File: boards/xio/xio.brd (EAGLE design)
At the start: 170 x 170 mm, 390 parts, among them U2 LAN8742A-CZ, Y1 NX3225SA-12.000MHZ-STD-CSR-1, Y2 NX3225SA-12.000MHZ-STD-CSR-1, Y3 NX3225SA-25.000MHZ-STD-CSR-1

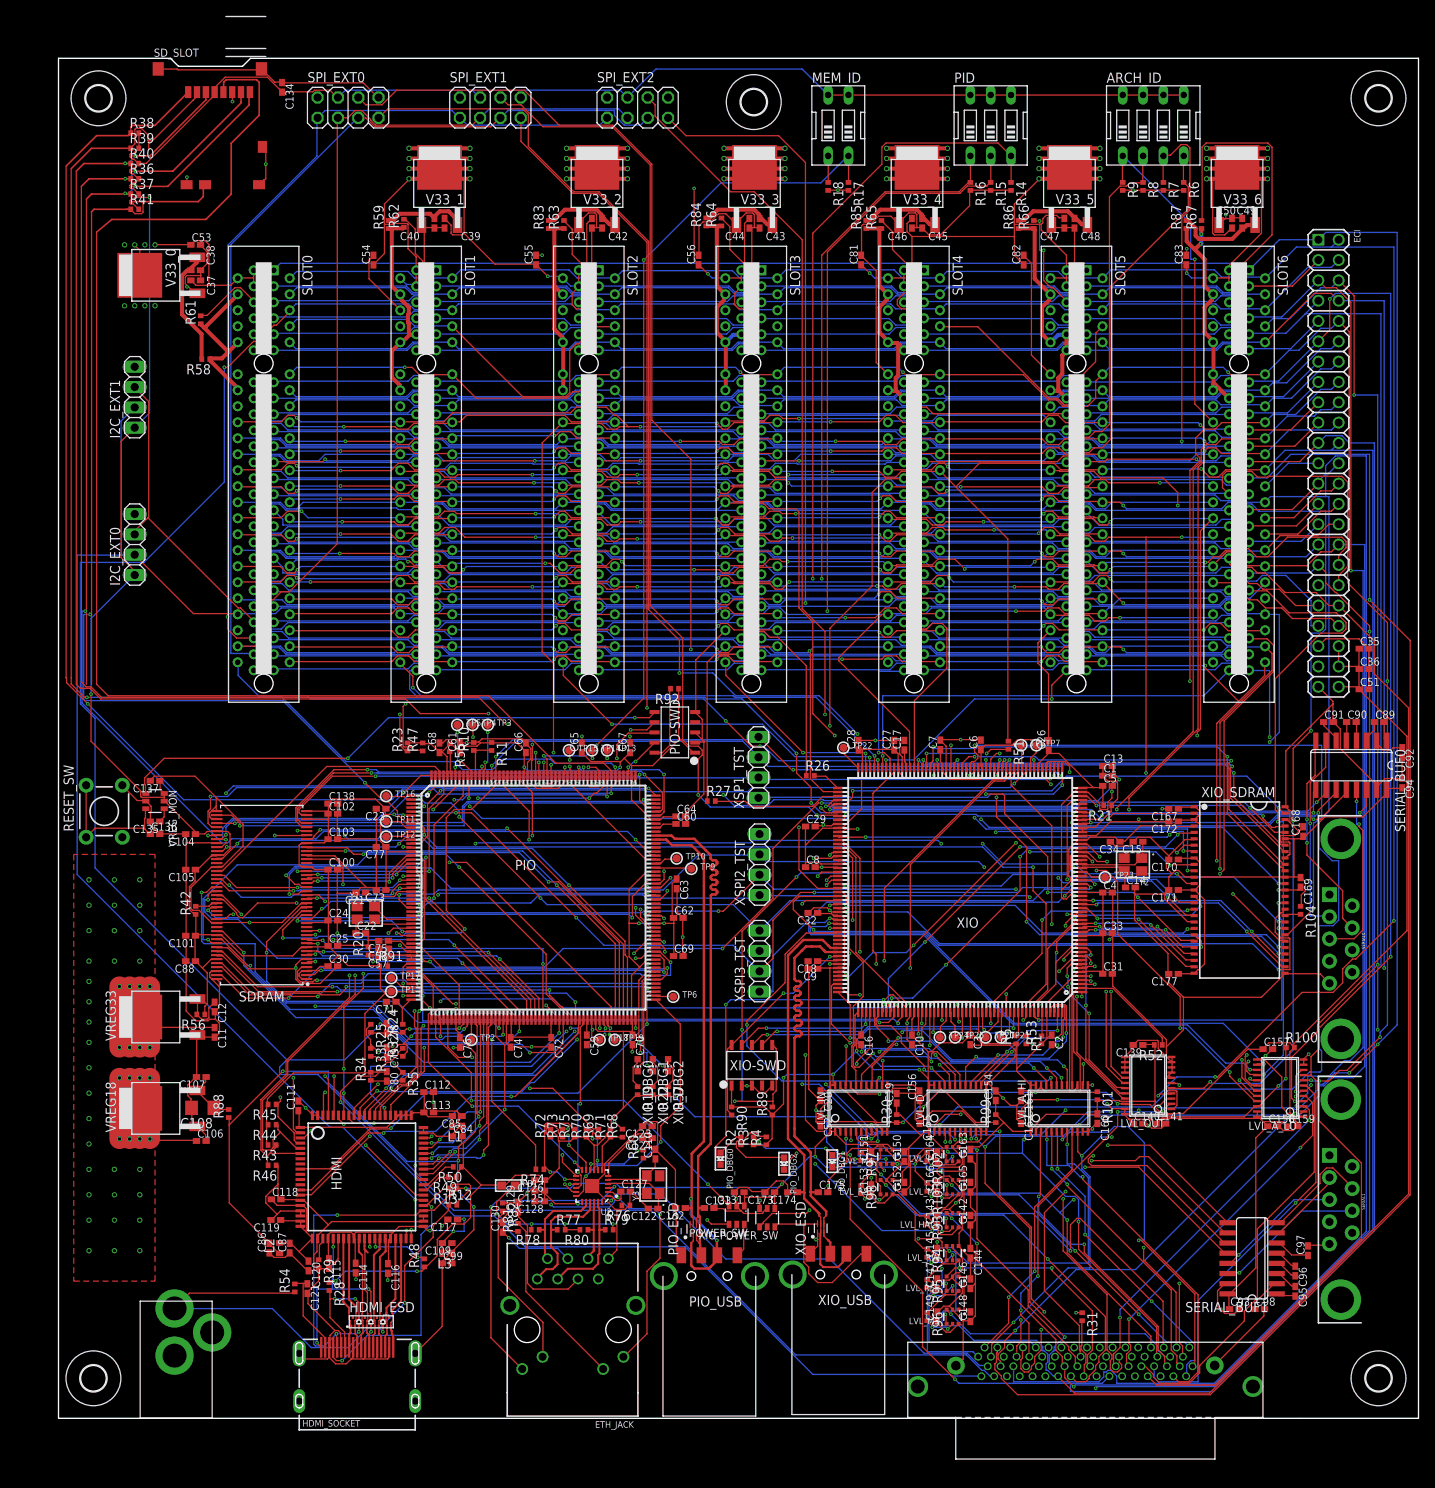
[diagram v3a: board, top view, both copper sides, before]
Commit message: Routed 6-layer board
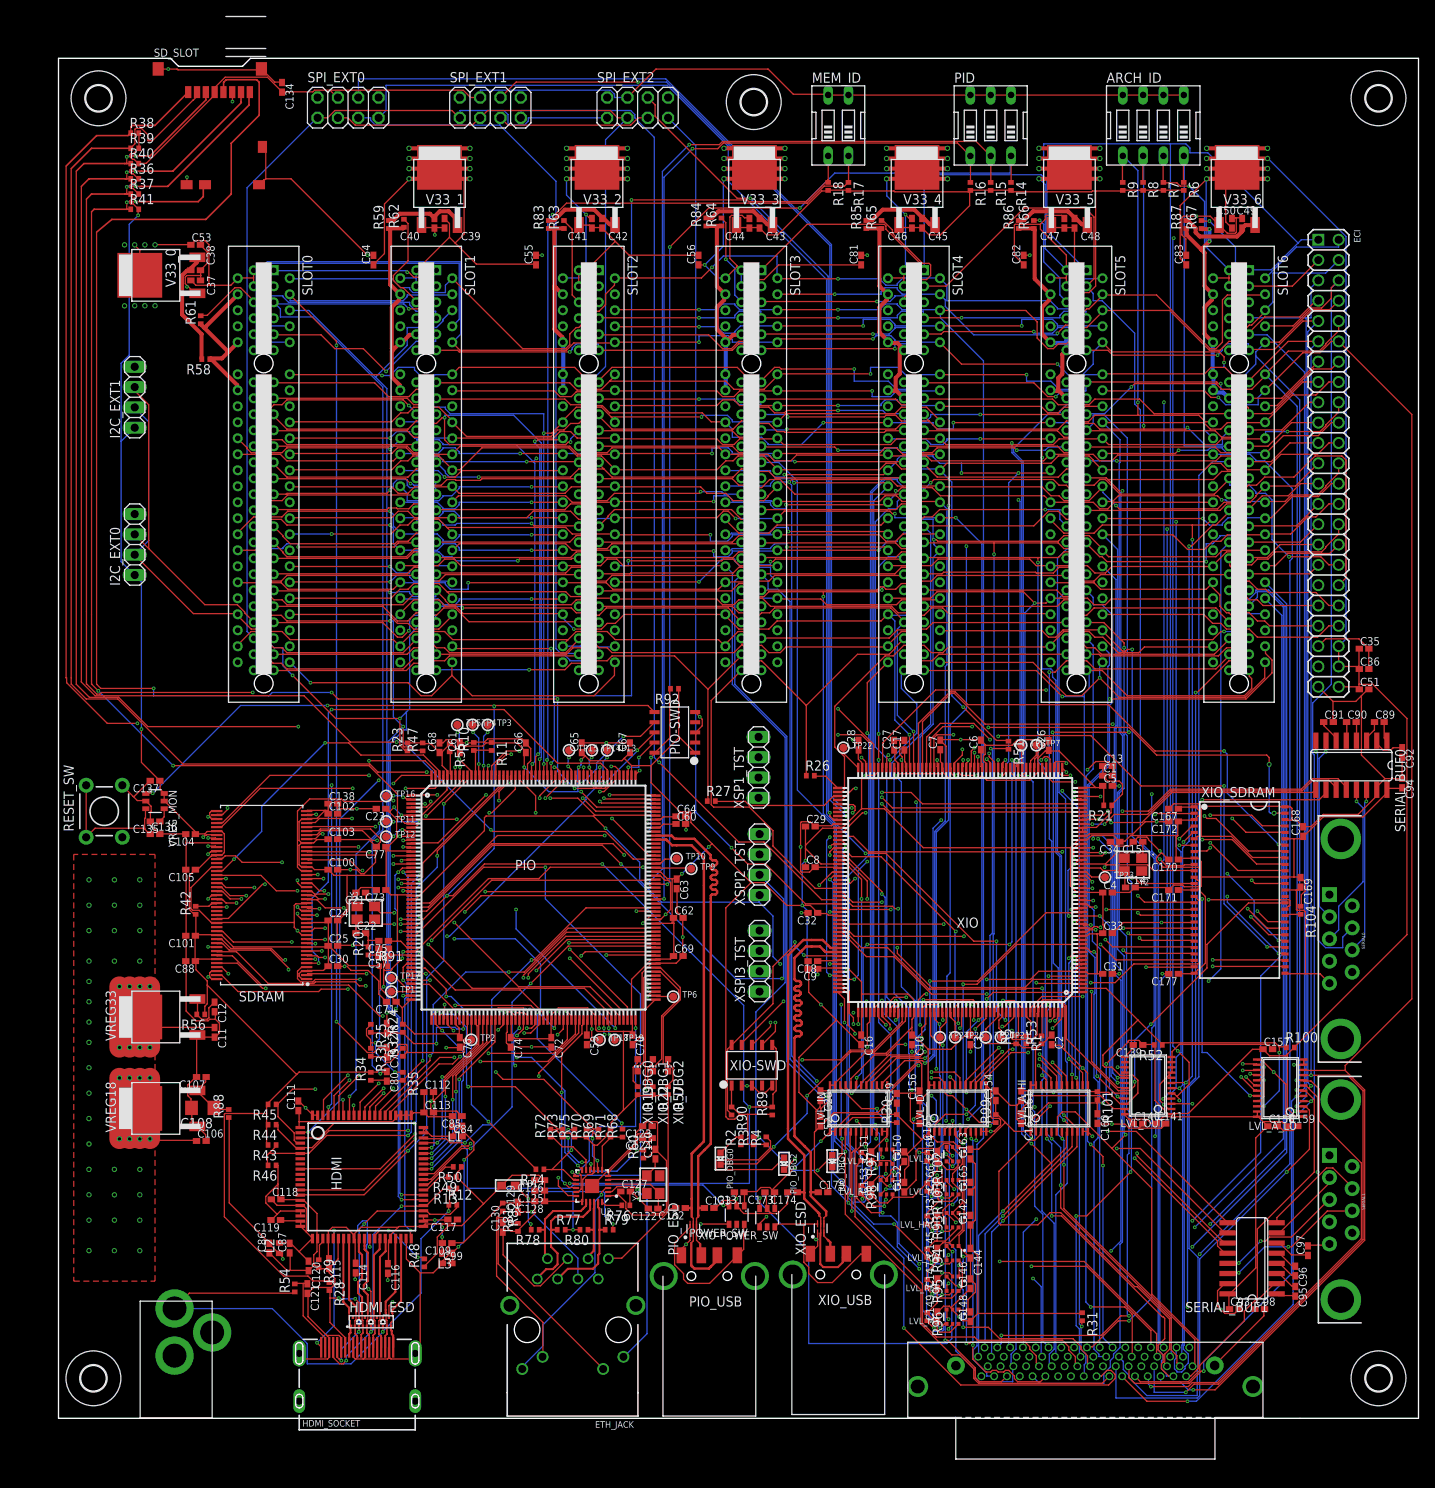
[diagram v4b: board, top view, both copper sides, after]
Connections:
- net GND: now also HDMI_ESD.P12; no longer HDMI_ESD.P18
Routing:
- net VHDCI_CCTL: track 346.4 -> 288.3 mm, vias 8 -> 3
- net VHDCI_CLK: track 328.5 -> 271.6 mm, vias 6 -> 4
- net VHDCI_COMMAND: track 305.3 -> 252.8 mm, vias 1 -> 4
- net VHDCI_D1: track 337.3 -> 288.2 mm, vias 1 -> 2
- net VHDCI_D0: track 301.8 -> 257.2 mm, vias 7 -> 5
- net I2C_SCL: track 314.0 -> 270.0 mm, vias 3 -> 6
- net VHDCI_HALT: track 294.2 -> 260.3 mm, vias 4 -> 2
- net GND: track 1203.2 -> 1169.5 mm, vias 75 -> 84
- net ETH_MDC: track 41.6 -> 73.2 mm
- net PSLOT6: track 40.0 -> 12.8 mm, vias 0 -> 1
- net VHDCI_A7: track 272.8 -> 299.9 mm, vias 1 -> 3
- net VHDCI_A3: track 292.9 -> 319.5 mm, vias 2 -> 5
- net VHDCI_A13: track 289.4 -> 263.4 mm, vias 7 -> 5
- net VHDCI_D4: track 268.8 -> 294.6 mm, vias 6 -> 3
- net VHDCI33_A9: track 62.1 -> 36.8 mm
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
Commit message: Big change.
Due to not being able to get the parts for the full system, we’re now just laying out the slots. We can add in the video and ethernet as cards rather than them being provided as-is.

This simplifies things a lot, now we only have 1 STM chip, and its associated SDRAM. The board is a lot smaller as well, and fits into 10cm in the Y dimension, which means making cards can be done using the cheap 10cm x 10cm board sizes that places like Seeed offer.

Need to define a cartridge port symbol, and remap all the pins to the STM32F746BGT6 (208 pin LQFP) which is available in China.

Assumption here is that the host-side will have an XPLA3 CPLD sitting on it, which manages the signal directionality under control of the STM, and also acts as a signal-buffer/level-translator. All signals on the expansion box are 3.3v apart from the 5v supply.

In the reverse direction, the STM ought to have sufficient juice to send the signals back on its own, since there’s only 1 load, and the signal path is short.
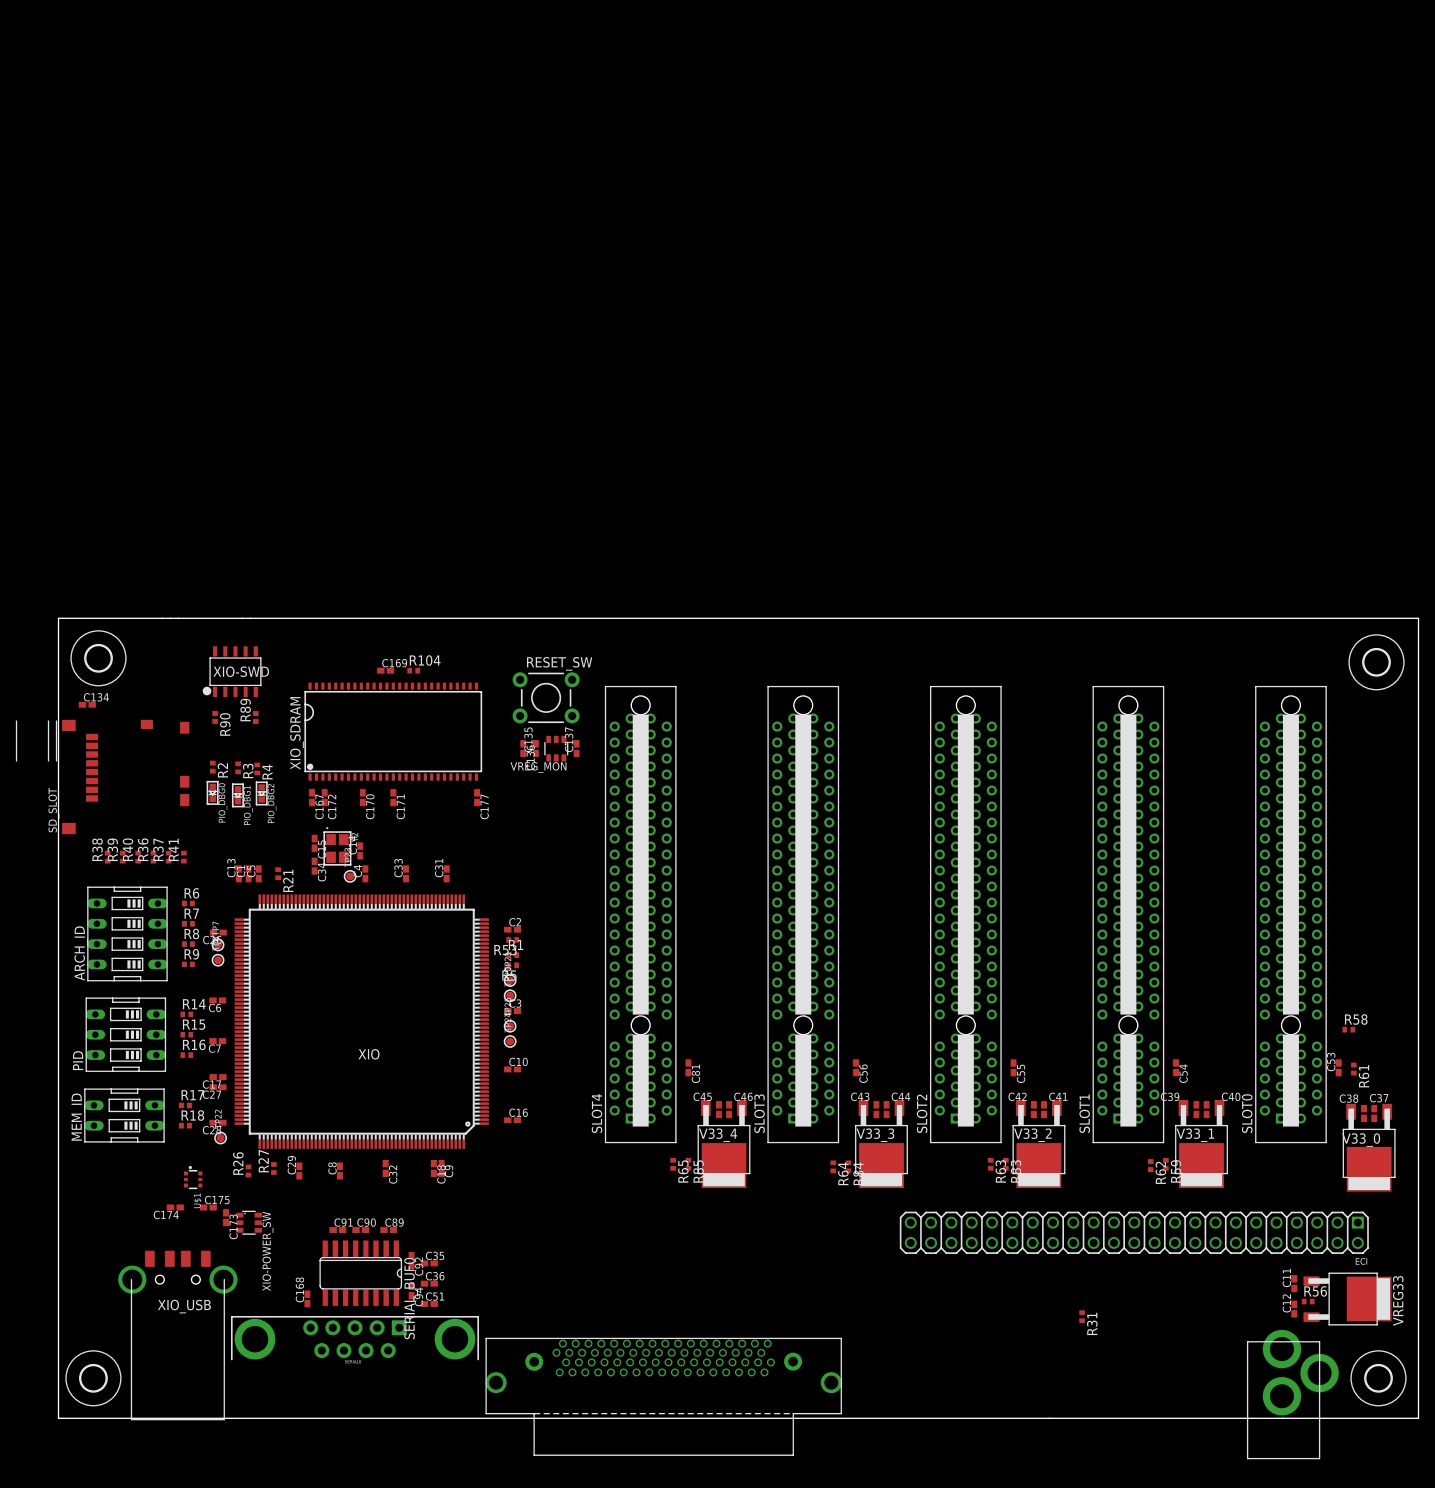
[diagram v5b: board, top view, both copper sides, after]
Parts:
- removed C100, C101, C102, C103, C104, C105, C109, C111, C112, C113, C114, C115, C116, C117, C118, C119, C120, C121, C125, C126, C127, C129, C130, C131, C139, C140, C142, C143, C144, C145, C146, C147, C148, C149, C150, C151, C152, C153, C154, C155, C157, C158, C160, C161, C163, C164, C165, C166, C19, C20, C23, C24, C25, C30, C58, C62, C63, C64, C65, C66, C67, C68, C69, C70, C71, C72, C73, C74, C75, C76, C77, C78, C79, C80, C82, C84, C85, C86, C87, C88, C93, C95, C96, C97, C98, C99: 0.1uF, rcl:C0402K
- removed C106, C107, C128, C47, C48, C49, C50, C57, C61, C83: 10uF, rcl:C0402K
- removed C108: 47uF, rcl:C1206
- removed C110, C122, C21, C22: 12pF, rcl:C0402K
- removed C123, C141, C156, C159, C162, C52: 1uF, rcl:C0402K
- removed C124: 470pF, rcl:C0402K
- removed C132, C133: 0.47pF, rcl:C0402K
- removed C138: 4.7uF, rcl:C0402K
- removed C59, C60: 2.2uF, rcl:C0402K
- removed ETH_JACK: J00-0065NL, microbuilder:RJ45_PULSEJACK
- removed FB1: BLM18PG221SN1D, microbuilder:0603
- removed H3: MOUNT-HOLE3.2, holes:3,2
- removed HDMI: ADV9889B, sjg-adv:LQFP80
- removed HDMI_ESD: MG2040, sjg-hdmi:UDFN18
- removed HDMI_SOCKET: 0471510001, microbuilder:HDMI_MOLEX_47151-0001
- removed I2C_EXT0, I2C_EXT1, XSP1_TST, XSPI2_TST, XSPI3_TST: (no value), pinhead:1X04
- removed L1, L2, L3: BLM15EG221SN1D, inductors:0402
- removed LVL_A_HI, LVL_A_LO, LVL_D, LVL_IN, LVL_OUT: SN74LVC8T245, sjg-logic:TSSOP24
- removed LVL_HALT, LVL_M3, LVL_M4, LVL_M5, LVL_M6, LVL_REF, LVL_RST, LVL_RW: 74LVC1T45GW,125, sjg-logic:SOT363
- removed PIO: STM32H753B-PIO, sjg-stm32:PQFP208
- removed PIO-SWD: FTSH-105-01-LM-DV-K, sjg-stm32:SWD_DEBUG
- removed PIO_ESD, XIO_ESD: RCLAMP0502N, sjg-usb:RESCAF40P120X100X65-6
- removed PIO_USB: USB-A, adafruit:MOLEX_480371000
- removed POWER_SW: NCP380, sjg-power:SOT23-6
- removed R10, R11, R20, R55: 0R, rcl:R0402
- removed R100, R101, R102, R103, R30, R52, R60, R93, R94, R95, R96, R97, R98, R99: 10k, rcl:R0402
- removed R12, R13, R23, R47: 2.7k, rcl:R0402
- removed R19, R22, R57: 1K, rcl:R0402
- removed R24, R25, R32, R33, R34, R35: 1k, rcl:R0402
- removed R28: 22K, rcl:R0402
- removed R29: 887.0 @ 1%, rcl:R0402
- removed R42, R44, R45, R66, R67, R70, R71, R72, R75, R92: 10K, rcl:R0402
- removed R43, R46: 100R, rcl:R0402
- removed R48, R49, R50: 4.7K, rcl:R0402
- removed R51, R91: 33, rcl:R0402
- removed R54: 10.0, rcl:R0402
- removed R68, R69, R73, R74: 33.0, rcl:R0402
- removed R76: 12.1K, rcl:R0402
- removed R77, R78, R79, R80: 49.9@1%, rcl:R0402
- removed R81, R82: 270, rcl:R0402
- removed R86, R87, R88: 0, rcl:R0402
- removed SDRAM: IS42S32800J, sjg-sdram:SOP50P1176X120-86
- removed SERIAL1: (no value), SparkFun:DB9
- removed SERIAL_BUF1: MAX3232CSE, maxim:SO16
- removed SLOT5, SLOT6: PCIE_98, pcie:PCI-E_98
- removed SPI_EXT0, SPI_EXT1, SPI_EXT2: (no value), pinhead:2X04
- removed TP1, TP10, TP11, TP12, TP13, TP14, TP15, TP16, TP17, TP18, TP19, TP2, TP3, TP4, TP5, TP6, TP9: (no value), microbuilder:TESTPOINT_ROUND_1MM
- removed U2: LAN8742A-CZ, microbuilder:QFN24_4MM
- removed V33_5, V33_6: AP7363-33D-13, sjg-power:TO252-3L
- removed VREG18: AP7363-18D-13, sjg-power:TO252-3L
- removed XIO_DBG0, XIO_DBG1, XIO_DBG2: ok33, led:CHIP-LED0603
- removed Y1: NX3225SA-12.000MHZ-STD-CSR-1, microbuilder:CRYSTAL_3.2X2.5
- removed Y3: NX3225SA-25.000MHZ-STD-CSR-1, microbuilder:CRYSTAL_3.2X2.5
- added U$1: PUSB2X4YH, sjg-isolation:SOT363
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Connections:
- removed net 1.8V: C84.2, C86.2, C99.2, L1.1, L2.1, L3.1, R88.1
- removed net 3V3_FILT: FB1.2, R77.2, R78.2, R79.2, R80.2
- removed net AUDIO_DATA: HDMI.9, PIO.107
- removed net AUDIO_SCLK: HDMI.13, PIO.90
- removed net AUDIO_WORD: HDMI.14, PIO.199
- removed net AVDD_9889B: C109.2, C114.1, C115.1, C116.1, C117.1, HDMI.24, HDMI.29, HDMI.36, HDMI.41, L3.2
- removed net CTS2: SERIAL1.8, SERIAL_BUF1.14
- removed net DIRN_OE: LVL_A_HI.22, LVL_A_LO.22, LVL_D.22, LVL_IN.22, LVL_OUT.22, R100.1, R101.1, R30.1, R52.1, R99.1, XIO.2
- removed net DIR_LVL0: LVL_HALT.5, R93.2, XIO.126
- removed net DIR_LVL1: LVL_RW.5, R94.2, XIO.127
- removed net DIR_LVL2: LVL_RST.5, R98.2, XIO.128
- removed net DIR_LVL3: LVL_REF.5, R95.2, XIO.186
- removed net DIR_LVL4: LVL_M3.5, R96.2, XIO.187
- removed net DIR_LVL5: LVL_M4.5, R97.2, XIO.188
- removed net DIR_LVL6: LVL_D.2, XIO.189
- removed net DIR_LVL7: LVL_A_HI.2, LVL_A_LO.2, XIO.190
- removed net DIR_LVL8: LVL_M5.5, R102.2, XIO.175
- removed net DIR_LVL9: LVL_M6.5, R103.2, XIO.176
- removed net DVDD_9889B: C111.1, C112.1, C113.1, C85.2, HDMI.1, HDMI.61, HDMI.62, HDMI.63, HDMI.64, L1.2
- removed net ETH_MDC: PIO.36, U2.13
- removed net ETH_MDIO: PIO.45, U2.12
- removed net ETH_RX_DV: R72.1, R73.1, U2.11
- removed net ETH_RX_N: ETH_JACK.6, R80.1, U2.22
- removed net ETH_RX_P: ETH_JACK.3, R79.1, U2.23
- removed net ETH_TXD0: PIO.104, U2.17
- removed net ETH_TX_D1: PIO.105, U2.18
- removed net ETH_TX_EN: PIO.91, U2.16
- removed net ETH_TX_N: ETH_JACK.2, R78.1, U2.20
- removed net ETH_TX_P: ETH_JACK.1, R77.1, U2.21
- removed net HDMI_CEC: HDMI_ESD.P17, HDMI_SOCKET.13, R28.2
- removed net HDMI_CLK_N: HDMI.27, HDMI_ESD.P1, HDMI_SOCKET.12
- removed net HDMI_CLK_P: HDMI.28, HDMI_ESD.P2, HDMI_SOCKET.10
- removed net HDMI_D0_N: HDMI.30, HDMI_ESD.P4, HDMI_SOCKET.9
- removed net HDMI_D0_P: HDMI.31, HDMI_ESD.P5, HDMI_SOCKET.7
- removed net HDMI_D1_N: HDMI.34, HDMI_ESD.P7, HDMI_SOCKET.6
- removed net HDMI_D1_P: HDMI.35, HDMI_ESD.P8, HDMI_SOCKET.4
- removed net HDMI_D2_N: HDMI.37, HDMI_ESD.P10, HDMI_SOCKET.3
- removed net HDMI_D2_P: HDMI.38, HDMI_ESD.P11, HDMI_SOCKET.1
- removed net HDMI_HPD: HDMI.25, HDMI_ESD.P15, HDMI_SOCKET.19
- removed net HDMI_IRQ: HDMI.40, PIO.43
- removed net HDMI_SCL: HDMI.44, HDMI_ESD.P3, HDMI_SOCKET.15, R12.2
- removed net HDMI_SDA: HDMI.45, HDMI_ESD.P6, HDMI_SOCKET.16, R13.2
- removed net LCD_B0: HDMI.2, PIO.174
- removed net LCD_B1: HDMI.78, PIO.175
- removed net LCD_B2: HDMI.77, PIO.176
- removed net LCD_B3: HDMI.76, PIO.177
- removed net LCD_B4: HDMI.75, PIO.186
- removed net LCD_B5: HDMI.74, PIO.187
- removed net LCD_B6: HDMI.73, PIO.188
- removed net LCD_B7: HDMI.72, PIO.189
- removed net LCD_CLK: HDMI.6, PIO.21, R43.1, R46.2
- removed net LCD_DE: HDMI.3, PIO.190
- removed net LCD_G0: HDMI.71, PIO.119
- removed net LCD_G1: HDMI.70, PIO.120
- removed net LCD_G2: HDMI.69, PIO.121
- removed net LCD_G3: HDMI.68, PIO.122
- removed net LCD_G4: HDMI.67, PIO.123
- removed net LCD_G5: HDMI.66, PIO.126
- removed net LCD_G6: HDMI.65, PIO.127
- removed net LCD_G7: HDMI.58, PIO.128
- removed net LCD_HSYNC: HDMI.4, PIO.19, R45.1
- removed net LCD_R0: HDMI.57, PIO.64
- removed net LCD_R1: HDMI.56, PIO.65
- removed net LCD_R2: HDMI.55, PIO.66
- removed net LCD_R3: HDMI.54, PIO.67
- removed net LCD_R4: HDMI.53, PIO.68
- removed net LCD_R5: HDMI.52, PIO.69
- removed net LCD_R6: HDMI.51, PIO.95
- removed net LCD_R7: HDMI.50, PIO.118
- removed net LCD_VSYNC: HDMI.5, PIO.20, R44.1
- removed net MISC0: PIO.46, XIO.166
- removed net MISC1: PIO.47, XIO.167
- removed net MISC2: PIO.48, XIO.168
- removed net N$100: PIO.167, TP13.P$1
- removed net N$101: PIO.168, TP14.P$1
- removed net N$102: PIO.173, TP15.P$1
- removed net N$103: PIO.2, TP16.P$1
- removed net N$104: PIO.49, TP17.P$1
- removed net N$105: PIO.96, TP18.P$1
- removed net N$106: PIO.97, TP19.P$1
- removed net N$134: C22.1, PIO.33, Y1.1
- removed net N$135: C21.1, PIO.32, Y1.2
- removed net N$17: PIO.111, XIO_DBG0.C
- removed net N$18: LVL_IN.3, R51.2
- removed net N$20: R19.1, XIO_DBG0.A
- removed net N$22: R22.1, XIO_DBG1.A
- removed net N$23: C79.2, PIO.62, R32.1, R33.2
- removed net N$24: R42.2, SDRAM.67
- removed net N$26: PIO.112, XIO_DBG1.C
- removed net N$27: PIO.113, XIO_DBG2.C
- removed net N$36: C80.2, PIO.31, R34.1, R35.2
- removed net N$38: HDMI.33, R48.2
- removed net N$4: C78.2, PIO.61, R24.1, R25.2
- removed net N$41: C97.1, SERIAL_BUF1.6
- removed net N$42: C98.1, SERIAL_BUF1.2
- removed net N$43: C95.2, SERIAL_BUF1.1
- removed net N$44: C95.1, SERIAL_BUF1.3
- removed net N$45: C96.1, SERIAL_BUF1.5
- removed net N$46: C96.2, SERIAL_BUF1.4
- removed net N$47: SERIAL_BUF1.11, XIO.182
- removed net N$48: SERIAL_BUF1.10, XIO.178
- removed net N$49: SERIAL_BUF1.12, XIO.183
- removed net N$50: SERIAL_BUF1.9, XIO.181
- removed net N$51: R57.1, XIO_DBG2.A
- removed net N$52: HDMI.48, R49.2
- removed net N$55: C48.1, R86.2, V33_5.P$3
- removed net N$56: C50.1, R87.2, V33_6.P$3
- removed net N$58: C107.1, C108.1, R88.2, VREG18.P$3
- removed net N$59: PIO_ESD.6, PIO_USB.1, POWER_SW.6
- removed net N$6: PIO.197, R10.1, R11.2
- removed net N$62: HDMI.49, R50.2
- removed net N$63: XIO-POWER_SW.6, XIO_ESD.6, XIO_USB.1
- removed net N$66: PIO.50, TP1.P$1
- removed net N$67: PIO.63, TP2.P$1
- removed net N$68: HDMI.23, R29.1
- removed net N$69: C121.1, HDMI_SOCKET.18, R54.2
- removed net N$70: PIO.195, TP3.P$1
- removed net N$71: PIO.196, TP4.P$1
- removed net N$72: PIO.198, TP5.P$1
- removed net N$73: PIO.106, TP6.P$1
- removed net N$74: R60.2, U2.10
- removed net N$75: PIO.58, R68.2
- removed net N$76: R68.1, R71.1, U2.7
- removed net N$77: PIO.57, R69.2
- removed net N$78: R69.1, R70.2, U2.8
- removed net N$79: PIO.56, R73.2
- removed net N$8: PIO.203, R55.2
- removed net N$80: PIO.44, R74.2
- removed net N$81: R74.1, R75.2, U2.14
- removed net N$82: C110.1, U2.5, Y3.2
- removed net N$83: C122.1, U2.4, Y3.1
- removed net N$84: R76.2, U2.24
- removed net N$85: C123.1, C124.1, U2.6
- removed net N$87: C129.1, ETH_JACK.5
- removed net N$88: C130.1, ETH_JACK.4
- removed net N$89: ETH_JACK.11, R81.2
- removed net N$90: ETH_JACK.9, U2.3
- removed net N$91: ETH_JACK.12, U2.2
- removed net N$92: ETH_JACK.10, R82.2
- removed net N$94: PIO.55, POWER_SW.4
- removed net N$95: PIO.54, POWER_SW.3
- removed net N$96: PIO.138, TP9.P$1
- removed net N$97: PIO.139, TP10.P$1
- removed net N$98: PIO.9, TP11.P$1
- removed net N$99: PIO.10, TP12.P$1
- removed net PIO_RX: PIO-SWD.P8, PIO.172
- removed net PIO_SWDCLK: PIO-SWD.P4, PIO.159
- removed net PIO_SWDIO: PIO-SWD.P2, PIO.147, R92.2
- removed net PIO_TX: PIO-SWD.P6, PIO.169
- removed net PIO_USB_N: C132.1, PIO.145, PIO_ESD.2, PIO_ESD.5, PIO_USB.2
- removed net PIO_USB_P: C133.1, PIO.146, PIO_ESD.3, PIO_ESD.4, PIO_USB.3
- removed net PIO_VDDA: C57.1, C58.1, PIO.41, PIO.42, R91.2
- removed net PSLOT5: R66.2, SLOT5.B5
- removed net PSLOT6: R67.2, SLOT6.B5
- removed net PVDD_9889B: C118.1, C119.1, C120.1, C87.2, HDMI.16, HDMI.19, HDMI.20, HDMI.21, L2.2
- removed net RTS2: SERIAL1.7, SERIAL_BUF1.8
- removed net RX2: SERIAL1.2, SERIAL_BUF1.7
- removed net S6_V33: R66.1, R86.1, SLOT5.B10, SLOT5.B11, SLOT5.B14, SLOT5.B15, SLOT5.B4, SLOT5.B9
- removed net S7_V33: R67.1, R87.1, SLOT6.B10, SLOT6.B12, SLOT6.B14, SLOT6.B15, SLOT6.B4
- removed net SPI_IRQ5: SLOT5.B48, XIO.152
- removed net SPI_IRQ6: SLOT6.B48, XIO.153
- removed net SPI_IRQ7: SPI_EXT0.7, XIO.194
- removed net SPI_IRQ8: SPI_EXT1.7, XIO.133
- removed net SPI_IRQ9: SPI_EXT2.7, XIO.134
- removed net SPI_SS5: SLOT5.B49, XIO.97
- removed net SPI_SS6: SLOT6.B49, XIO.98
- removed net SPI_SS7: SPI_EXT0.6, XIO.111
- removed net SPI_SS8: SPI_EXT1.6, XIO.112
- removed net SPI_SS9: SPI_EXT2.6, XIO.113
- removed net STM_RAM_A0: PIO.16, SDRAM.25
- removed net STM_RAM_A1: PIO.17, SDRAM.26
- removed net STM_RAM_A10: PIO.77, SDRAM.24
- removed net STM_RAM_A11: PIO.78, SDRAM.21
- removed net STM_RAM_A2: PIO.18, SDRAM.27
- removed net STM_RAM_A3: PIO.22, SDRAM.60
- removed net STM_RAM_A4: PIO.23, SDRAM.61
- removed net STM_RAM_A5: PIO.24, SDRAM.62
- removed net STM_RAM_A6: PIO.71, SDRAM.63
- removed net STM_RAM_A7: PIO.74, SDRAM.64
- removed net STM_RAM_A8: PIO.75, SDRAM.65
- removed net STM_RAM_A9: PIO.76, SDRAM.66
- removed net STM_RAM_BA0: PIO.131, SDRAM.22
- removed net STM_RAM_BA1: PIO.132, SDRAM.23
- removed net STM_RAM_CAS: PIO.191, SDRAM.18
- removed net STM_RAM_CLK: PIO.135, SDRAM.68
- removed net STM_RAM_D0: PIO.116, SDRAM.2
- removed net STM_RAM_D1: PIO.117, SDRAM.4
- removed net STM_RAM_D10: PIO.87, SDRAM.77
- removed net STM_RAM_D11: PIO.88, SDRAM.79
- removed net STM_RAM_D12: PIO.89, SDRAM.80
- removed net STM_RAM_D13: PIO.108, SDRAM.82
- removed net STM_RAM_D14: PIO.109, SDRAM.83
- removed net STM_RAM_D15: PIO.110, SDRAM.85
- removed net STM_RAM_D16: PIO.98, SDRAM.31
- removed net STM_RAM_D17: PIO.99, SDRAM.33
- removed net STM_RAM_D18: PIO.100, SDRAM.34
- removed net STM_RAM_D19: PIO.101, SDRAM.36
- removed net STM_RAM_D2: PIO.164, SDRAM.5
- removed net STM_RAM_D20: PIO.102, SDRAM.37
- removed net STM_RAM_D21: PIO.151, SDRAM.39
- removed net STM_RAM_D22: PIO.152, SDRAM.40
- removed net STM_RAM_D23: PIO.153, SDRAM.42
- removed net STM_RAM_D24: PIO.154, SDRAM.45
- removed net STM_RAM_D25: PIO.155, SDRAM.47
- removed net STM_RAM_D26: PIO.156, SDRAM.48
- removed net STM_RAM_D27: PIO.157, SDRAM.50
- removed net STM_RAM_D28: PIO.207, SDRAM.51
- removed net STM_RAM_D29: PIO.208, SDRAM.53
- removed net STM_RAM_D3: PIO.165, SDRAM.7
- removed net STM_RAM_D30: PIO.11, SDRAM.54
- removed net STM_RAM_D31: PIO.12, SDRAM.56
- removed net STM_RAM_D4: PIO.79, SDRAM.8
- removed net STM_RAM_D5: PIO.80, SDRAM.10
- removed net STM_RAM_D6: PIO.81, SDRAM.11
- removed net STM_RAM_D7: PIO.84, SDRAM.13
- removed net STM_RAM_D8: PIO.85, SDRAM.74
- removed net STM_RAM_D9: PIO.86, SDRAM.76
- removed net STM_RAM_DQM0: PIO.200, SDRAM.16
- removed net STM_RAM_DQM1: PIO.201, SDRAM.71
- removed net STM_RAM_DQM2: PIO.205, SDRAM.28
- removed net STM_RAM_DQM3: PIO.206, SDRAM.59
- removed net STM_RAM_RAS: PIO.70, SDRAM.19
- removed net STM_RAM_WE: PIO.35, SDRAM.17
- removed net TX2: SERIAL1.3, SERIAL_BUF1.13
- removed net VCAP1: C59.1, PIO.92
- removed net VCAP2: C60.1, PIO.148
- removed net VHDCI33_A0: LVL_A_LO.21, XIO.35
- removed net VHDCI33_A1: LVL_A_LO.20, XIO.36
- removed net VHDCI33_A10: LVL_A_HI.19, XIO.161
- removed net VHDCI33_A11: LVL_A_HI.18, XIO.162
- removed net VHDCI33_A12: LVL_A_HI.17, XIO.163
- removed net VHDCI33_A13: LVL_A_HI.16, XIO.8
- removed net VHDCI33_A14: LVL_A_HI.15, XIO.9
- removed net VHDCI33_A15: LVL_A_HI.14, XIO.10
- removed net VHDCI33_A2: LVL_A_LO.19, XIO.37
- removed net VHDCI33_A3: LVL_A_LO.18, XIO.38
- removed net VHDCI33_A4: LVL_A_LO.17, XIO.57
- removed net VHDCI33_A5: LVL_A_LO.16, XIO.58
- removed net VHDCI33_A6: LVL_A_LO.15, XIO.138
- removed net VHDCI33_A7: LVL_A_LO.14, XIO.139
- removed net VHDCI33_A8: LVL_A_HI.21, XIO.140
- removed net VHDCI33_A9: LVL_A_HI.20, XIO.141
- removed net VHDCI33_CCTL: LVL_IN.20, XIO.7
- removed net VHDCI33_CLK: LVL_IN.21, XIO.65
- removed net VHDCI33_D0: LVL_D.21, XIO.154
- removed net VHDCI33_D1: LVL_D.20, XIO.155
- removed net VHDCI33_D1XX: LVL_IN.17, XIO.11
- removed net VHDCI33_D2: LVL_D.19, XIO.156
- removed net VHDCI33_D3: LVL_D.18, XIO.157
- removed net VHDCI33_D4: LVL_D.17, XIO.205
- removed net VHDCI33_D5: LVL_D.16, XIO.206
- removed net VHDCI33_D6: LVL_D.15, XIO.207
- removed net VHDCI33_D7: LVL_D.14, XIO.208
- removed net VHDCI33_EXSEL: LVL_OUT.20, XIO.12
- removed net VHDCI33_HALT: LVL_HALT.4, XIO.13
- removed net VHDCI33_IRQ: LVL_OUT.19, XIO.19
- removed net VHDCI33_MPD: LVL_OUT.21, XIO.20
- removed net VHDCI33_RD4: LVL_IN.16, XIO.21
- removed net VHDCI33_RD5: LVL_IN.15, XIO.64
- removed net VHDCI33_REF: LVL_REF.4, XIO.66
- removed net VHDCI33_RSRVD0: LVL_IN.14, XIO.67
- removed net VHDCI33_RSRVD1: LVL_OUT.18, XIO.68
- removed net VHDCI33_RSRVD2: LVL_OUT.17, XIO.69
- removed net VHDCI33_RSRVD3: LVL_M3.4, XIO.95
- removed net VHDCI33_RSRVD4: LVL_M4.4, XIO.118
- removed net VHDCI33_RSRVD5: LVL_M5.4, XIO.119
- removed net VHDCI33_RSRVD6: LVL_M6.4, XIO.120
- removed net VHDCI33_RST: LVL_RST.4, XIO.121
- removed net VHDCI33_RW: LVL_RW.4, XIO.122
- removed net VHDCI33_S4: LVL_IN.19, XIO.123
- removed net VHDCI33_S5: LVL_IN.18, XIO.174
- removed net XSPI1_CLK: PIO.192, XIO.54, XSP1_TST.4
- removed net XSPI1_MISO: PIO.193, XIO.55, XSP1_TST.3
- removed net XSPI1_MOSI: PIO.194, XIO.56, XSP1_TST.2
- removed net XSPI1_SSEL: PIO.53, XIO.53, XSP1_TST.1
- removed net XSPI2_CLK: PIO.28, XIO.1, XSPI2_TST.4
- removed net XSPI2_IRQ: PIO.13, XIO.62
- removed net XSPI2_MISO: PIO.29, XIO.4, XSPI2_TST.3
- removed net XSPI2_MOSI: PIO.30, XIO.5, XSPI2_TST.2
- removed net XSPI2_SSEL: PIO.27, XIO.3, XSPI2_TST.1
- removed net XSPI3_CLK: PIO.1, XIO.28, XSPI3_TST.4
- removed net XSPI3_IRQ: PIO.7, XIO.198
- removed net XSPI3_MISO: PIO.4, XIO.29, XSPI3_TST.3
- removed net XSPI3_MOSI: PIO.5, XIO.30, XSPI3_TST.2
- removed net XSPI3_SSEL: PIO.3, XIO.27, XSPI3_TST.1
- new net XIO_USB_VBUS: U$1.6, XIO-POWER_SW.6, XIO_USB.1
- net !RESET!: no longer PIO-SWD.P10, PIO.34, U2.15
- net !VHDCI_EXSEL!: now also XIO.68; no longer LVL_OUT.4, SLOT5.A1, SLOT6.A1
- net !VHDCI_IRQ!: now also XIO.69; no longer LVL_OUT.5, SLOT5.A2, SLOT6.A2
- net !VHDCI_MPD!: now also XIO.67; no longer LVL_OUT.3, SLOT5.A3, SLOT6.A3
- net +3V3: no longer C100.1, C101.1, C102.1, C103.1, C104.1, C105.1, C125.1, C126.1, C127.1, C128.1, C138.1, C140.1, C141.1, C143.1, C145.1, C147.1, C149.1, C151.1, C153.1, C155.1, C156.1, C158.1, C159.1, C161.1, C162.1, C164.1, C166.1, C20.1, C23.1, C24.1, C25.1, C30.1, C52.1, C61.1, C62.1, C63.1, C64.1, C65.1, C66.1, C67.1, C68.1, C69.1, C70.1, C71.1, C72.1, C73.1, C74.1, C75.1, C76.1, C77.1, C88.1, C93.1, FB1.1, I2C_EXT0.1, I2C_EXT1.1, LVL_A_HI.23, LVL_A_HI.24, LVL_A_LO.23, LVL_A_LO.24, LVL_D.23, LVL_D.24, LVL_HALT.6, LVL_IN.23, LVL_IN.24, LVL_M3.6, LVL_M4.6, LVL_M5.6, LVL_M6.6, LVL_OUT.23, LVL_OUT.24, LVL_REF.6, LVL_RST.6, LVL_RW.6, PIO-SWD.P1, PIO.103, PIO.115, PIO.124, PIO.137, PIO.15, PIO.150, PIO.158, PIO.171, PIO.185, PIO.204, PIO.26, PIO.39, PIO.52, PIO.59, PIO.6, PIO.73, PIO.83, PIO.94, R102.1, R103.1, R11.1, R19.2, R22.2, R23.2, R24.2, R28.1, R32.2, R34.2, R42.1, R43.2, R44.2, R45.2, R47.2, R48.1, R49.1, R50.1, R55.1, R57.2, R70.1, R71.2, R72.2, R75.1, R91.1, R92.1, R93.1, R94.1, R95.1, R96.1, R97.1, R98.1, SDRAM.1, SDRAM.15, SDRAM.29, SDRAM.3, SDRAM.35, SDRAM.41, SDRAM.43, SDRAM.49, SDRAM.55, SDRAM.75, SDRAM.81, SDRAM.9, SERIAL_BUF1.16, SPI_EXT0.4, SPI_EXT1.4, SPI_EXT2.4, U2.1, U2.19, U2.9
- net +5V: no longer C106.1, C131.1, C139.1, C142.2, C144.2, C146.2, C148.2, C150.2, C152.2, C154.1, C157.1, C160.1, C163.2, C165.2, C19.1, C47.1, C49.1, C82.1, C83.1, HDMI_ESD.P9, LVL_A_HI.1, LVL_A_LO.1, LVL_D.1, LVL_HALT.1, LVL_IN.1, LVL_IN.2, LVL_M3.1, LVL_M4.1, LVL_M5.1, LVL_M6.1, LVL_OUT.1, LVL_REF.1, LVL_RST.1, LVL_RW.1, POWER_SW.1, R100.2, R101.2, R12.1, R13.1, R30.2, R52.2, R54.1, R99.2, SLOT5.B1, SLOT5.B2, SLOT5.B3, SLOT6.B1, SLOT6.B2, SLOT6.B3, V33_5.P$1, V33_6.P$1, VREG18.P$1
- net AGND: no longer C57.2, C58.2, PIO.40, R20.1, R25.1, R33.1, R35.1
- net ARCH0: no longer PIO.180, SLOT5.B18, SLOT6.B18
- net ARCH1: no longer PIO.181, SLOT5.B19, SLOT6.B19
- net ARCH2: no longer PIO.182, SLOT5.B20, SLOT6.B20
- net ARCH3: no longer PIO.183, SLOT5.B21, SLOT6.B21
- net A_OK: no longer SLOT5.B17, SLOT6.B17
- net GND: now also U$1.2; no longer C100.2, C101.2, C102.2, C103.2, C104.2, C105.2, C106.2, C107.2, C108.2, C109.1, C110.2, C111.2, C112.2, C113.2, C114.2, C115.2, C116.2, C117.2, C118.2, C119.2, C120.2, C121.2, C122.2, C123.2, C124.2, C125.2, C126.2, C127.2, C128.2, C129.2, C130.2, C131.2, C132.2, C133.2, C138.2, C139.2, C140.2, C141.2, C142.1, C143.2, C144.1, C145.2, C146.1, C147.2, C148.1, C149.2, C150.1, C151.2, C152.1, C153.2, C154.2, C155.2, C156.2, C157.2, C158.2, C159.2, C160.2, C161.2, C162.2, C163.1, C164.2, C165.1, C166.2, C19.2, C20.2, C21.2, C22.2, C23.2, C24.2, C25.2, C30.2, C47.2, C48.2, C49.2, C50.2, C52.2, C59.2, C60.2, C61.2, C62.2, C63.2, C64.2, C65.2, C66.2, C67.2, C68.2, C69.2, C70.2, C71.2, C72.2, C73.2, C74.2, C75.2, C76.2, C77.2, C82.2, C83.2, C84.1, C85.1, C86.1, C87.1, C88.2, C93.2, C97.2, C98.2, C99.1, ETH_JACK.7, ETH_JACK.8, HDMI.15, HDMI.17, HDMI.18, HDMI.22, HDMI.26, HDMI.32, HDMI.39, HDMI.42, HDMI.43, HDMI.59, HDMI.60, HDMI.79, HDMI.80, HDMI_ESD.P12, HDMI_SOCKET.11, HDMI_SOCKET.14, HDMI_SOCKET.17, HDMI_SOCKET.2, HDMI_SOCKET.5, HDMI_SOCKET.8, HDMI_SOCKET.P$1, HDMI_SOCKET.P$2, HDMI_SOCKET.P$3, HDMI_SOCKET.P$4, I2C_EXT0.4, I2C_EXT1.4, LVL_A_HI.11, LVL_A_HI.12, LVL_A_HI.13, LVL_A_LO.11, LVL_A_LO.12, LVL_A_LO.13, LVL_D.11, LVL_D.12, LVL_D.13, LVL_HALT.2, LVL_IN.11, LVL_IN.12, LVL_IN.13, LVL_M3.2, LVL_M4.2, LVL_M5.2, LVL_M6.2, LVL_OUT.10, LVL_OUT.11, LVL_OUT.12, LVL_OUT.13, LVL_OUT.14, LVL_OUT.15, LVL_OUT.16, LVL_OUT.2, LVL_OUT.8, LVL_OUT.9, LVL_REF.2, LVL_RST.2, LVL_RW.2, PIO-SWD.P3, PIO-SWD.P5, PIO-SWD.P9, PIO.114, PIO.125, PIO.136, PIO.14, PIO.149, PIO.170, PIO.184, PIO.202, PIO.25, PIO.51, PIO.60, PIO.72, PIO.82, PIO.93, PIO_ESD.1, PIO_USB.4, POWER_SW.2, R10.2, R20.2, R29.2, R46.1, R60.1, R76.1, R81.1, R82.1, SDRAM.12, SDRAM.20, SDRAM.32, SDRAM.38, SDRAM.44, SDRAM.46, SDRAM.52, SDRAM.58, SDRAM.6, SDRAM.72, SDRAM.78, SDRAM.84, SDRAM.86, SERIAL1.5, SERIAL_BUF1.15, SLOT5.B12, SLOT5.B13, SLOT5.B16, SLOT5.B41, SLOT5.B44, SLOT5.B6, SLOT5.B7, SLOT5.B8, SLOT6.B11, SLOT6.B13, SLOT6.B16, SLOT6.B41, SLOT6.B44, SLOT6.B6, SLOT6.B7, SLOT6.B8, SLOT6.B9, SPI_EXT0.8, SPI_EXT1.8, SPI_EXT2.8, U2.THERM, V33_5.P$2, V33_6.P$2, VREG18.P$2, XIO_ESD.1
- net I2C_SCL: no longer HDMI.46, I2C_EXT0.2, I2C_EXT1.2, R47.1, SLOT5.B42, SLOT6.B42
- net I2C_SDA: no longer HDMI.47, I2C_EXT0.3, I2C_EXT1.3, R23.1, SLOT5.B43, SLOT6.B43
- net MEM0: no longer PIO.178
- net MEM1: no longer PIO.179
- net PID0: no longer PIO.130
- net PID1: no longer PIO.133
- net PID2: no longer PIO.134
- net SD0: no longer PIO.140
- net SD1: no longer PIO.141
- net SD2: no longer PIO.161
- net SD3: no longer PIO.162
- net SDCD: no longer PIO.8
- net SDCLK: no longer PIO.163
- net SDCMD: no longer PIO.166
- net SPI_CLK: no longer SLOT5.B45, SLOT6.B45, SPI_EXT0.1, SPI_EXT1.1, SPI_EXT2.1
- net SPI_IRQ4: no longer XIO.151
- net SPI_MISO: no longer SLOT5.B46, SLOT6.B46, SPI_EXT0.3, SPI_EXT1.3, SPI_EXT2.3
- net SPI_MOSI: no longer SLOT5.B47, SLOT6.B47, SPI_EXT0.5, SPI_EXT1.5, SPI_EXT2.5
- net VHDCI_A0: now also XIO.35; no longer LVL_A_LO.3, SLOT5.A7, SLOT6.A7
- net VHDCI_A1: now also XIO.36; no longer LVL_A_LO.4, SLOT5.A8, SLOT6.A8
- net VHDCI_A10: now also XIO.161; no longer LVL_A_HI.5, SLOT5.A17, SLOT6.A17
- net VHDCI_A11: now also XIO.162; no longer LVL_A_HI.6, SLOT5.A18, SLOT6.A18
- net VHDCI_A12: now also XIO.163; no longer LVL_A_HI.7, SLOT5.A19, SLOT6.A19
- net VHDCI_A13: now also XIO.8; no longer LVL_A_HI.8, SLOT5.A20, SLOT6.A20
- net VHDCI_A14: now also XIO.9; no longer LVL_A_HI.9, SLOT5.A21, SLOT6.A21
- net VHDCI_A15: now also XIO.10; no longer LVL_A_HI.10, SLOT5.A22, SLOT6.A22
- net VHDCI_A2: now also XIO.37; no longer LVL_A_LO.5, SLOT5.A9, SLOT6.A9
- net VHDCI_A3: now also XIO.38; no longer LVL_A_LO.6, SLOT5.A10, SLOT6.A10
- net VHDCI_A4: now also XIO.57; no longer LVL_A_LO.7, SLOT5.A11, SLOT6.A11
- net VHDCI_A5: now also XIO.58; no longer LVL_A_LO.8, SLOT5.A12, SLOT6.A12
- net VHDCI_A6: now also XIO.138; no longer LVL_A_LO.9, SLOT5.A13, SLOT6.A13
- net VHDCI_A7: now also XIO.139; no longer LVL_A_LO.10, SLOT5.A14, SLOT6.A14
- net VHDCI_A8: now also XIO.140; no longer LVL_A_HI.3, SLOT5.A15, SLOT6.A15
- net VHDCI_A9: now also XIO.141; no longer LVL_A_HI.4, SLOT5.A16, SLOT6.A16
- net VHDCI_AUDIO_L: no longer C79.1, SLOT5.A4, SLOT6.A4
- net VHDCI_AUDIO_R: no longer C80.1, SLOT5.A5, SLOT6.A5
- net VHDCI_AUDIO_SIO: no longer C78.1, SLOT5.A6, SLOT6.A6
- net VHDCI_CCTL: now also XIO.95; no longer LVL_IN.4, SLOT5.A23, SLOT6.A23
- net VHDCI_CLK: now also XIO.65; no longer R51.1, SLOT5.A24, SLOT6.A24
- net VHDCI_COMMAND: no longer SLOT5.A25, SLOT6.A25
- net VHDCI_D0: now also XIO.154; no longer LVL_D.3, SLOT5.A28, SLOT6.A28
- net VHDCI_D1: now also XIO.155; no longer LVL_D.4, SLOT5.A29, SLOT6.A29
- net VHDCI_D1XX: now also XIO.121; no longer LVL_IN.7, SLOT5.A26, SLOT6.A26
- net VHDCI_D2: now also XIO.156; no longer LVL_D.5, SLOT5.A30, SLOT6.A30
- net VHDCI_D3: now also XIO.157; no longer LVL_D.6, SLOT5.A31, SLOT6.A31
- net VHDCI_D4: now also XIO.205; no longer LVL_D.7, SLOT5.A32, SLOT6.A32
- net VHDCI_D5: now also XIO.206; no longer LVL_D.8, SLOT5.A33, SLOT6.A33
- net VHDCI_D6: now also XIO.207; no longer LVL_D.9, SLOT5.A34, SLOT6.A34
- net VHDCI_D7: now also XIO.208; no longer LVL_D.10, SLOT5.A35, SLOT6.A35
- net VHDCI_DATA_OUT: no longer SLOT5.A27, SLOT6.A27
- net VHDCI_GND: no longer SLOT5.A36, SLOT6.A36
- net VHDCI_HALT: now also XIO.123; no longer LVL_HALT.3, SLOT5.A37, SLOT6.A37
- net VHDCI_J1_1: no longer SLOT5.A40, SLOT6.A40
- net VHDCI_J1_2: no longer SLOT5.A41, SLOT6.A41
- net VHDCI_J1_3: no longer SLOT5.A42, SLOT6.A42
- net VHDCI_J1_4: no longer SLOT5.A43, SLOT6.A43
- net VHDCI_J1_5: no longer SLOT5.A44, SLOT6.A44
- net VHDCI_J1_A1: no longer SLOT5.A38, SLOT6.A38
- net VHDCI_J1_A2: no longer SLOT5.A39, SLOT6.A39
- net VHDCI_J2_1: no longer SLOT5.A47, SLOT6.A47
- net VHDCI_J2_2: no longer SLOT5.A48, SLOT6.A48
- net VHDCI_J2_3: no longer SLOT5.A49, SLOT6.A49
- net VHDCI_J2_4: no longer SLOT5.B22, SLOT6.B22
- net VHDCI_J2_5: no longer SLOT5.B23, SLOT6.B23
- net VHDCI_J2_A1: no longer SLOT5.A45, SLOT6.A45
- net VHDCI_J2_A2: no longer SLOT5.A46, SLOT6.A46
- net VHDCI_MTR_CTRL: no longer SLOT5.B24, SLOT6.B24
- net VHDCI_RD4: now also XIO.66; no longer LVL_IN.8, SLOT5.B25, SLOT6.B25
- net VHDCI_RD5: now also XIO.64; no longer LVL_IN.9, SLOT5.B26, SLOT6.B26
- net VHDCI_REF: now also XIO.120; no longer LVL_REF.3, SLOT5.B27, SLOT6.B27
- net VHDCI_RSRVD0: now also XIO.7; no longer LVL_IN.10, SLOT5.B28, SLOT6.B28
- net VHDCI_RSRVD1: now also XIO.11; no longer LVL_OUT.6, SLOT5.B29, SLOT6.B29
- net VHDCI_RSRVD2: now also XIO.12; no longer LVL_OUT.7, SLOT5.B30, SLOT6.B30
- net VHDCI_RSRVD3: now also XIO.13; no longer LVL_M3.3, SLOT5.B31, SLOT6.B31
- net VHDCI_RSRVD4: now also XIO.19; no longer LVL_M4.3, SLOT5.B32, SLOT6.B32
- net VHDCI_RSRVD5: now also XIO.20; no longer LVL_M5.3, SLOT5.B33, SLOT6.B33
- net VHDCI_RSRVD6: now also XIO.21; no longer LVL_M6.3, SLOT5.B34, SLOT6.B34
- net VHDCI_RST: now also XIO.122; no longer LVL_RST.3, SLOT5.B35, SLOT6.B35
- net VHDCI_RW: now also XIO.174; no longer LVL_RW.3, SLOT5.B36, SLOT6.B36
- net VHDCI_S4: now also XIO.119; no longer LVL_IN.5, SLOT5.B37, SLOT6.B37
- net VHDCI_S5: now also XIO.118; no longer LVL_IN.6, SLOT5.B38, SLOT6.B38
- net VHDCI_SIO_CLK_IN: no longer SLOT5.B39, SLOT6.B39
- net VHDCI_SIO_DATA_IN: no longer SLOT5.B40, SLOT6.B40
- net XIO_USB_N: now also U$1.3; no longer XIO_ESD.2, XIO_ESD.5
- net XIO_USB_P: now also U$1.4; no longer XIO_ESD.3, XIO_ESD.4
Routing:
- net +3V3: track 1253.5 -> 0.00 mm, vias 14 -> 0
- net GND: track 1169.5 -> 0.00 mm, vias 84 -> 0
- net +5V: track 789.1 -> 0.00 mm, vias 117 -> 0
- net VHDCI_AUDIO_SIO: track 375.1 -> 0.00 mm, vias 3 -> 0
- net !VHDCI_EXSEL!: track 343.6 -> 0.00 mm, vias 3 -> 0
- net VHDCI_AUDIO_L: track 342.1 -> 0.00 mm, vias 4 -> 0
- net VHDCI_AUDIO_R: track 324.8 -> 0.00 mm, vias 3 -> 0
- net VHDCI_A1: track 322.7 -> 0.00 mm, vias 5 -> 0
- net VHDCI_A3: track 319.5 -> 0.00 mm, vias 5 -> 0
- net !VHDCI_IRQ!: track 311.7 -> 0.00 mm, vias 5 -> 0
- net !VHDCI_MPD!: track 308.4 -> 0.00 mm, vias 2 -> 0
- net VHDCI_A0: track 304.3 -> 0.00 mm, vias 5 -> 0
- net VHDCI_RW: track 302.6 -> 0.00 mm, vias 1 -> 0
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- removed copper zone on layer 15, net +3V3
- removed copper zone on layer 1, net +5V
- removed copper zone on layer 15, net +5V
- removed copper zone on layer 2, net GND
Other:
- board size 170 x 170 mm -> 170 x 100 mm
- board text added: "Indent SD card slot Make parts for STM32F Neaten everything up Make cartridge part 5650118-1 and place Add 5v plane rectangle Add GND plane Add 3.3v plane Find better (larger) USB ESD part"
